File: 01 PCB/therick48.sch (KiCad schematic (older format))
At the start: 133 parts, among them J1 TYPE-C-31-M12_13, J2 AVR-ISP-6_mod, K1 KEYSW, K10 KEYSW, K11 KEYSW, K12 KEYSW, K13 KEYSW, K14 KEYSW, K15 KEYSW, K16 KEYSW, K17 KEYSW, K18 KEYSW, K19 KEYSW, K2 KEYSW, K20 KEYSW, K21 KEYSW, K22 KEYSW, K23 KEYSW, K24 KEYSW, K25 KEYSW, K26 KEYSW, K27 KEYSW, K28 KEYSW, K29 KEYSW, K3 KEYSW, K30 KEYSW, K31 KEYSW, K32 KEYSW, K33 KEYSW, K34 KEYSW, K35 KEYSW, K36 KEYSW, K37 KEYSW, K38 KEYSW, K39 KEYSW, K4 KEYSW, K40 KEYSW, K41 KEYSW, K42 KEYSW, K43 KEYSW, K44 KEYSW, K45 KEYSW, K46 KEYSW, K47 KEYSW, K48 KEYSW, K5 KEYSW, K6 KEYSW, K7 KEYSW, K8 KEYSW, K9 KEYSW, SW1 SW_PUSH, U1 ATMEGA32U4, U2 HOLE, U3 USBLC6-2SC6, U4 HOLE, Y1 16MHz

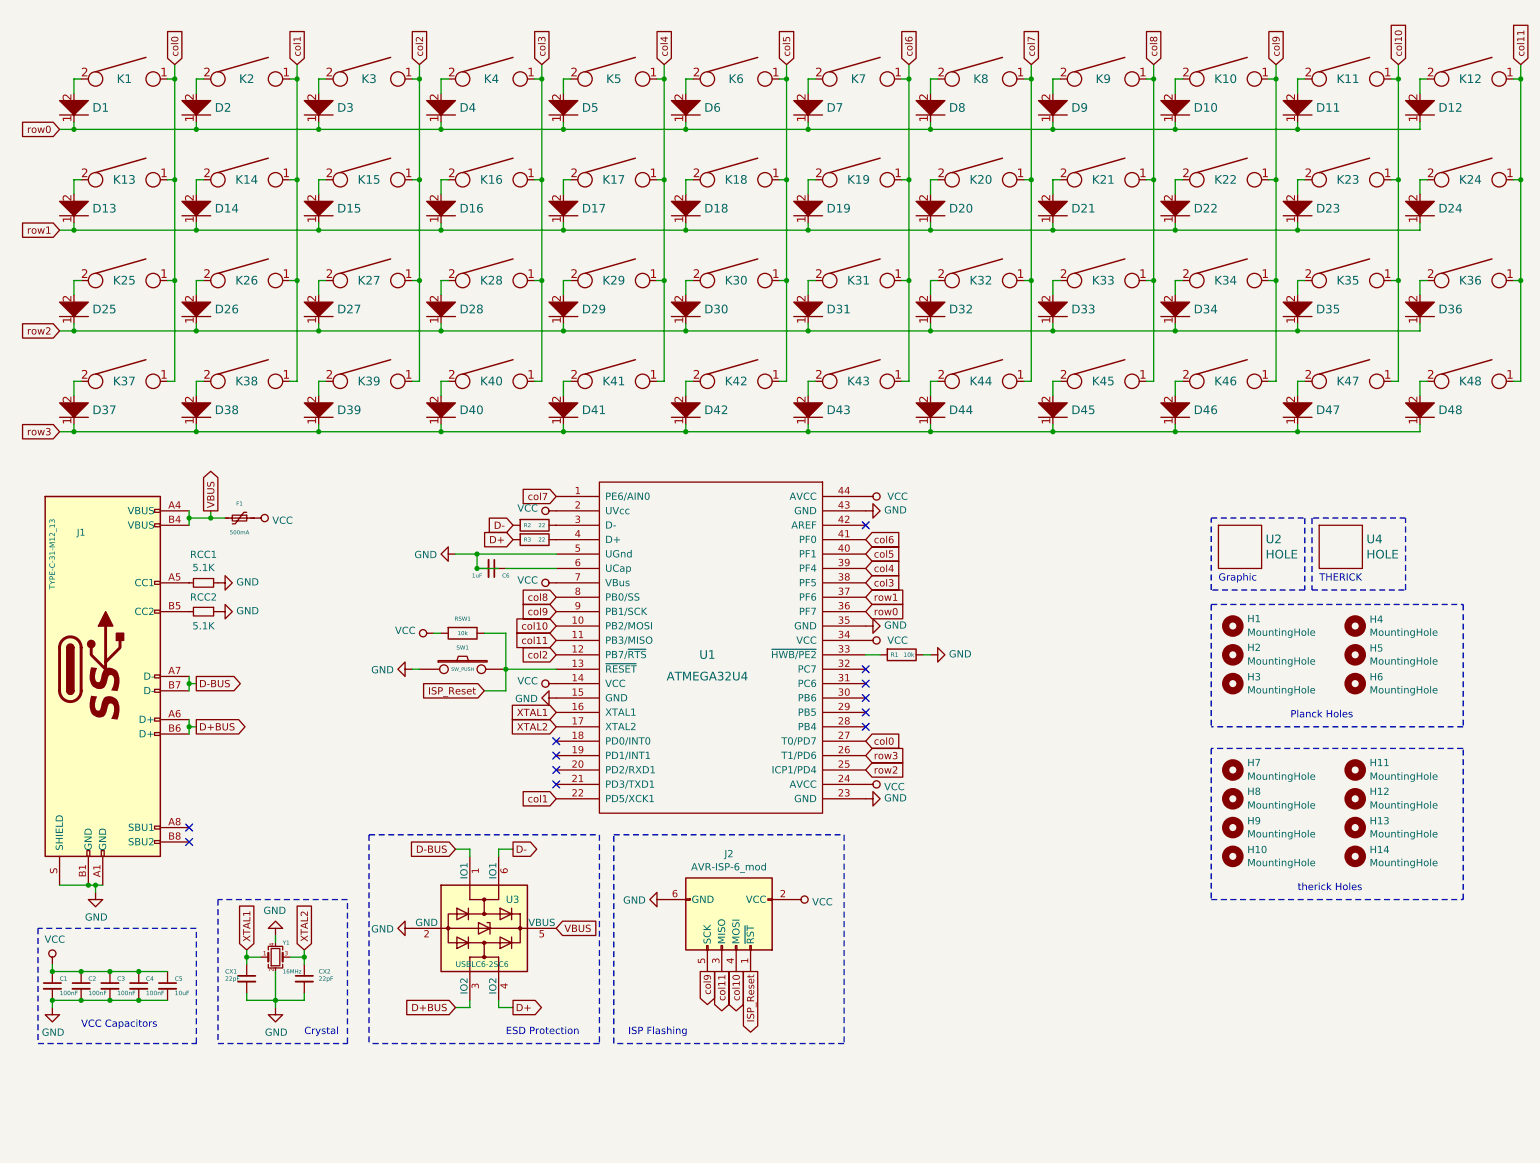
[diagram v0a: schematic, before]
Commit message: Add power LED
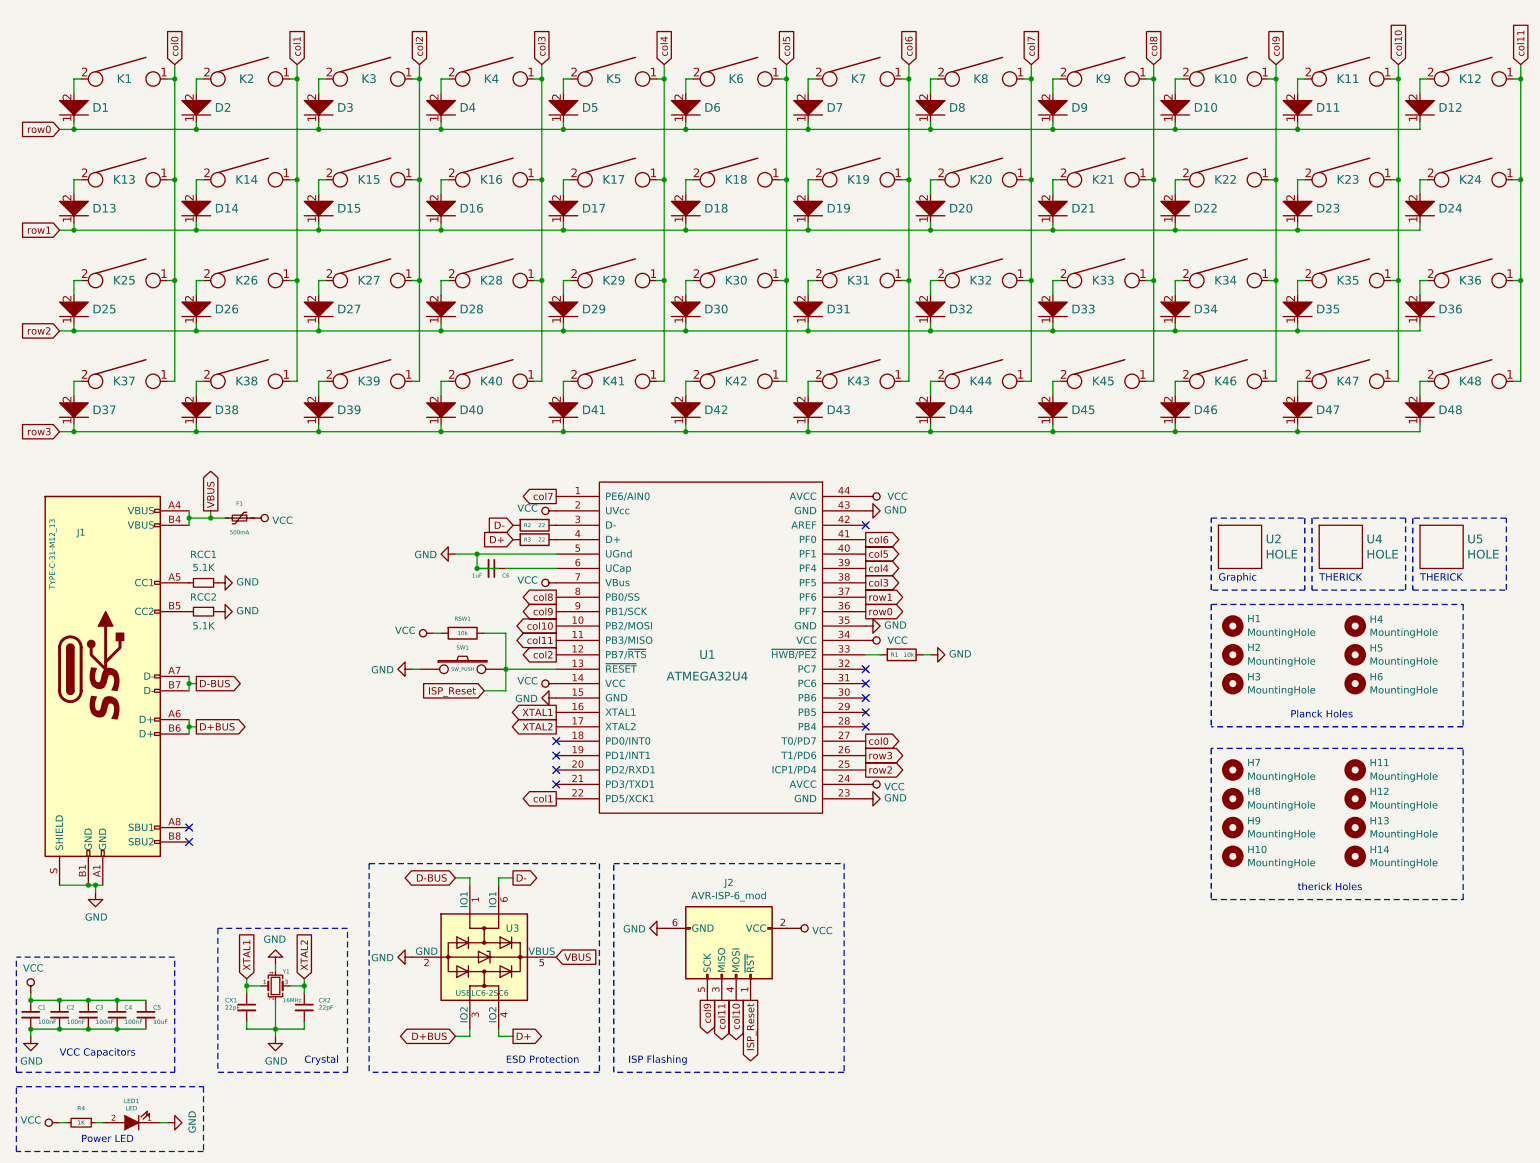
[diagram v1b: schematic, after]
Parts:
- added LED1: LED, LED_SMD:LED_0805_2012Metric_Pad1.15x1.40mm_HandSolder, symbol keyboard_parts:LED
- added R4: 1K, Resistor_SMD:R_0805_2012Metric_Pad1.15x1.40mm_HandSolder, symbol Device:R_Small
- added U5: HOLE, Symbol:OSHW-Logo2_9.8x8mm_SilkScreen, symbol lets_split-cache:HOLE
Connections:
- net GND: now also LED1.1 (K)
- net VCC: now also R4.2
- new net: LED1.2 (A), R4.1
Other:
- note added: "Power LED"
- moved on the sheet: C1, C2, C3, C4, C5, CX1, CX2, J2, U3, Y1

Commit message: Gerber
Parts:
- U5: footprint Symbol:OSHW-Logo2_9.8x8mm_SilkScreen -> Symbol:OSHW-Logo_11.4x12mm_SilkScreen
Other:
- note added: "Open Hardware"
- moved on the sheet: C1, C2, C3, C4, C5, CX1, CX2, LED1, R4, Y1
